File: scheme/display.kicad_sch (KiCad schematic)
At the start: 21 parts, among them M1 Fan_4pin, M2 Fan_4pin, M3 Fan_4pin, U30 T-Display-S3, U32 EMC2302-1, U33 TXU0102-DCU, U37 TMP1075, U38 TMP1075

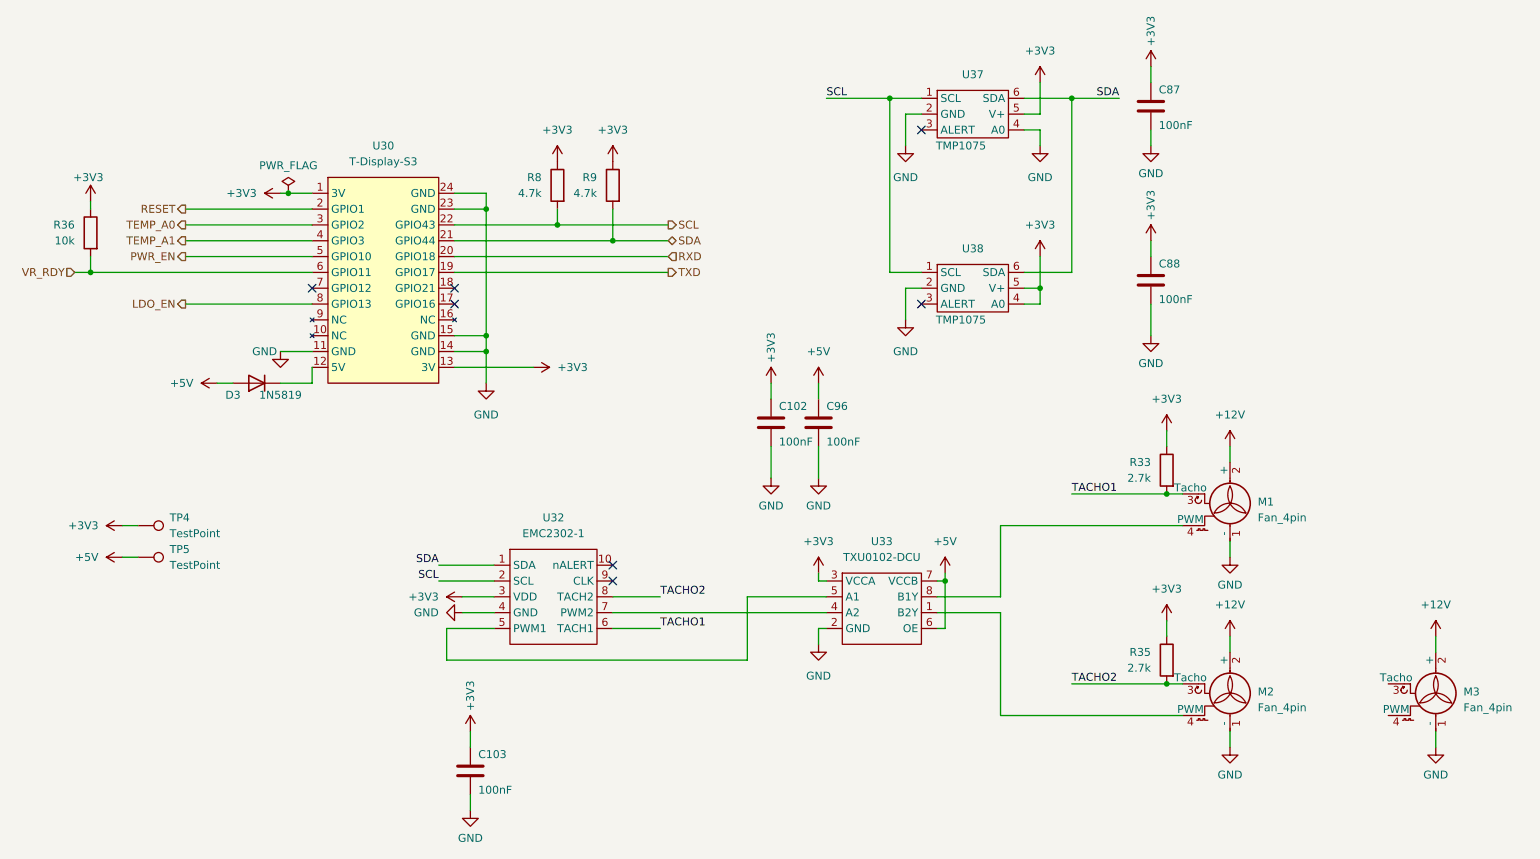
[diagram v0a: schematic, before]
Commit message: Updated schematics with correct cap rating
We upgraded certain capacitors to a higher nF rating and have changed the schematic to reflect it so the BOM can be generated accurately.
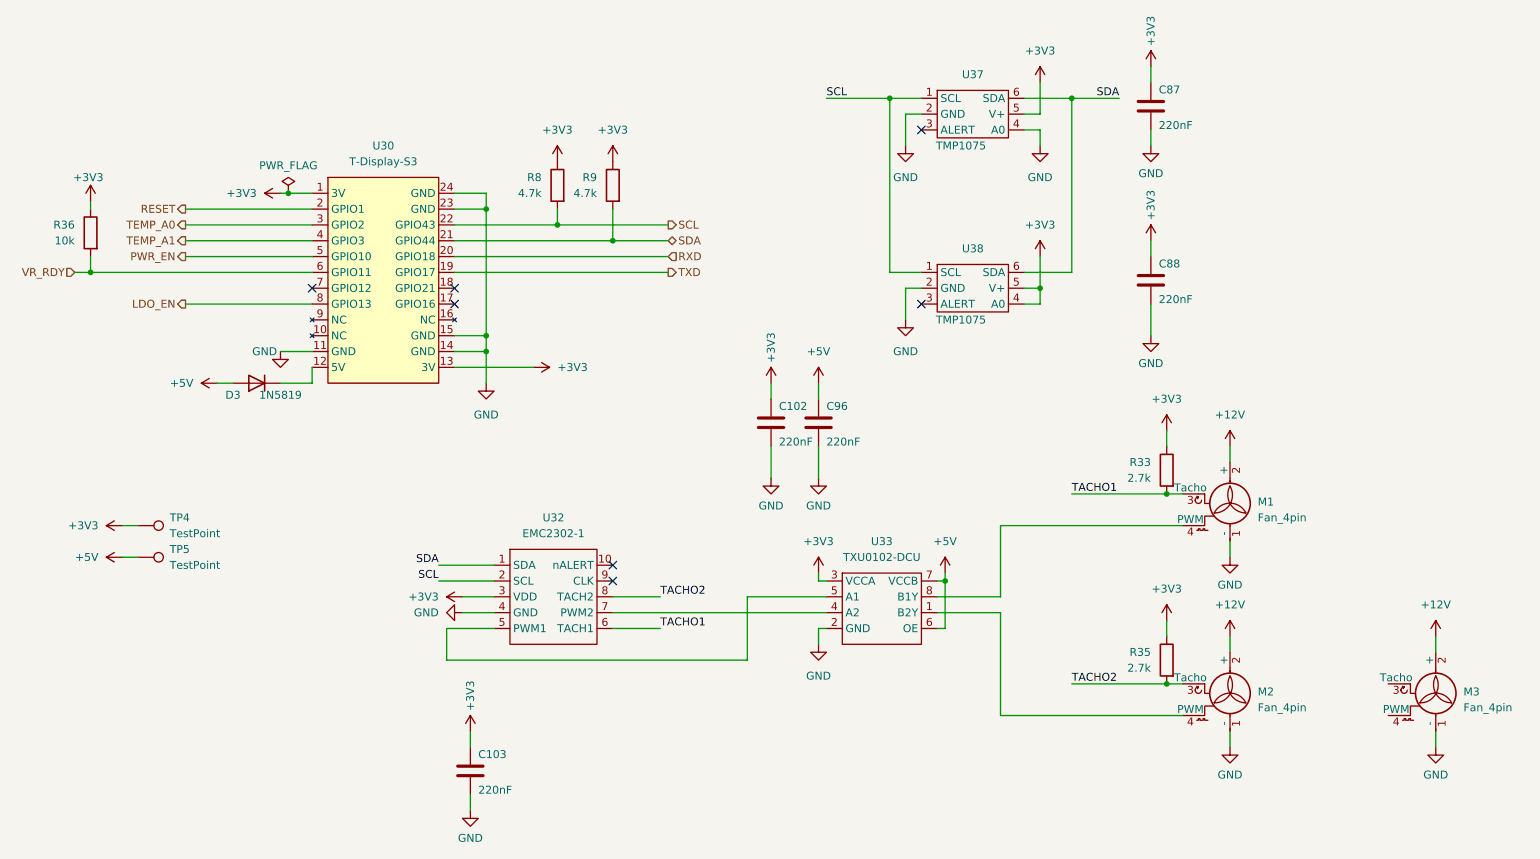
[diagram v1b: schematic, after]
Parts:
- C102, C103, C87, C88, C96: value 100nF -> 220nF
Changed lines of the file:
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@@
 			)
 		)
-		(property "Value" "100nF"
+		(property "Value" "220nF"
 			(at 212.09 62.23 0)
 			(effects
@@
 			)
 		)
-		(property "Value" "100nF"
+		(property "Value" "220nF"
 			(at 212.09 34.29 0)
 			(effects
@@
 			)
 		)
-		(property "Value" "100nF"
+		(property "Value" "220nF"
 			(at 151.13 85.09 0)
 			(effects
@@
 			)
 		)
-		(property "Value" "100nF"
+		(property "Value" "220nF"
 			(at 102.87 140.97 0)
 			(effects
@@
 			)
 		)
-		(property "Value" "100nF"
+		(property "Value" "220nF"
 			(at 158.75 85.09 0)
 			(effects
